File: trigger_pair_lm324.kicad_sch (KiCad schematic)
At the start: 53 parts, among them J6 AudioJack2, J7 AudioJack2, U11 1SS362FV_L3F, U12 1SS362FV_L3F, U13 LM324, U14 1SS362FV_L3F, U15 1SS362FV_L3F, U16 1SS362FV_L3F, U17 1SS362FV_L3F, U18 LM324

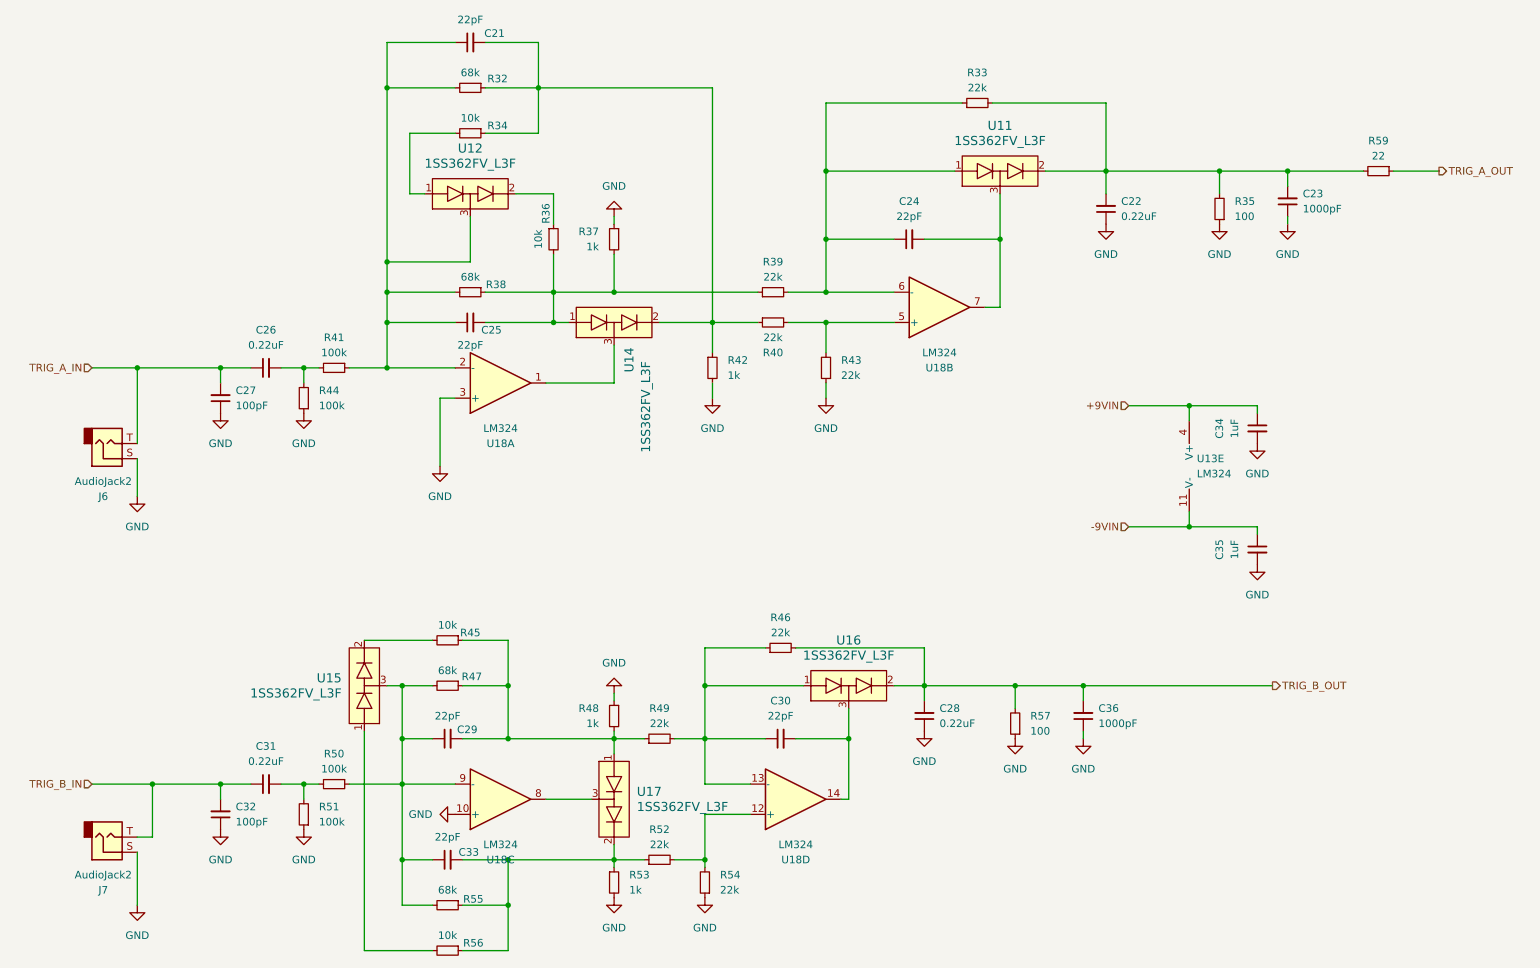
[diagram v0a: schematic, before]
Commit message: Double trigger layout to test
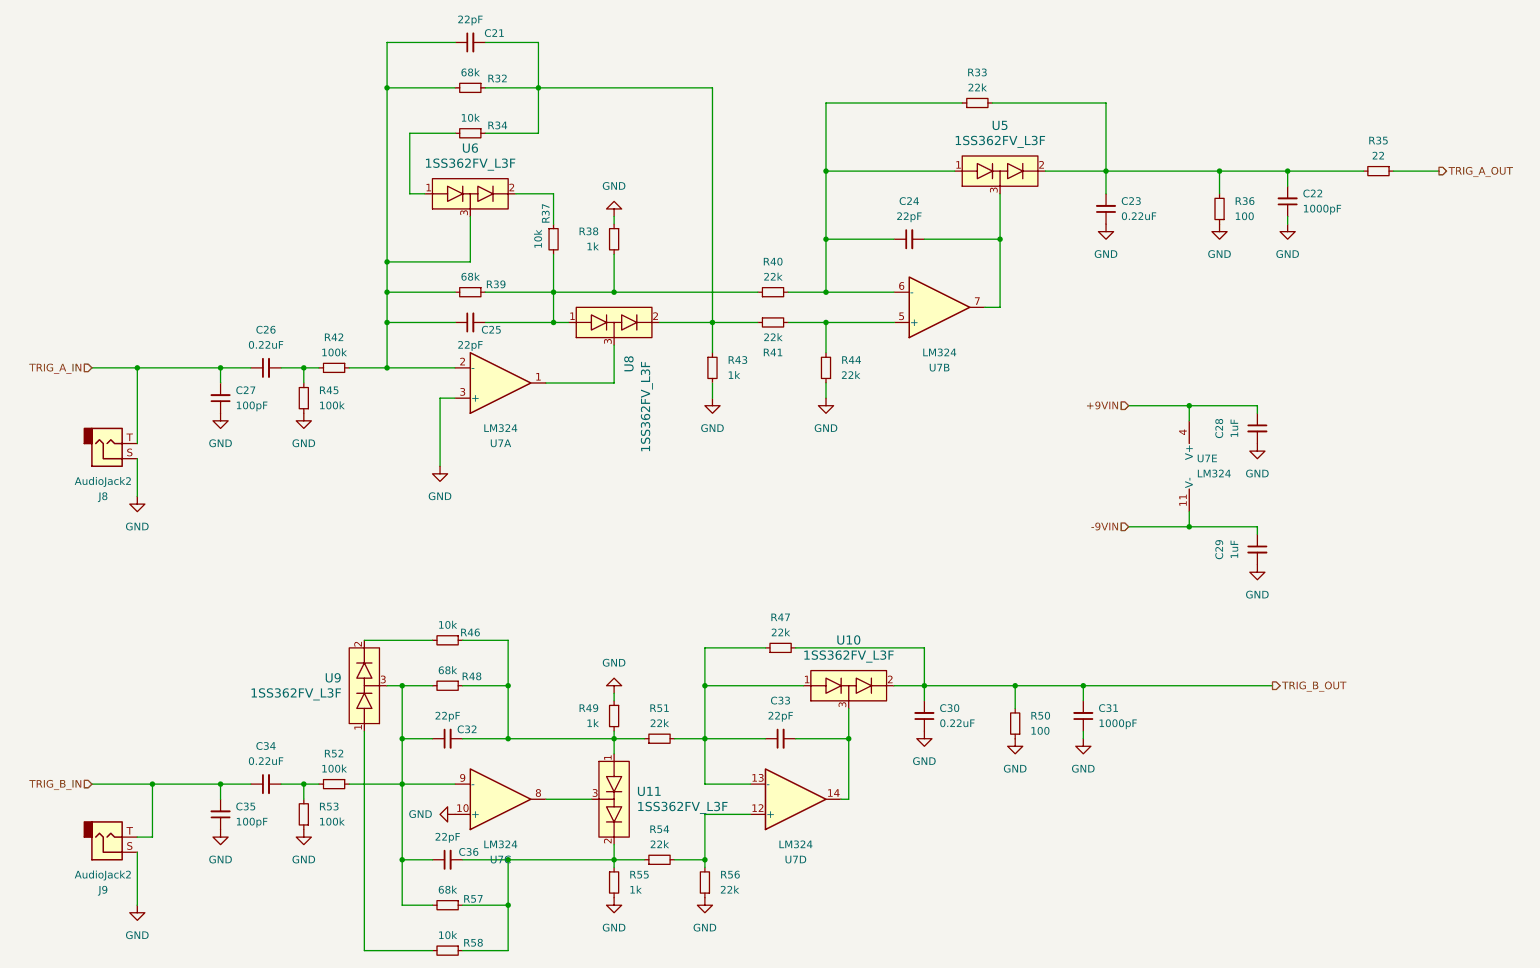
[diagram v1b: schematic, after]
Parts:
- C21, C24, C25: footprint Capacitor_SMD:C_0402_1005Metric -> C_0402_custom:C_0402_1005Metric
- C32: renamed from C29; footprint Capacitor_SMD:C_0402_1005Metric -> C_0402_custom:C_0402_1005Metric
- C33: renamed from C30; footprint Capacitor_SMD:C_0402_1005Metric -> C_0402_custom:C_0402_1005Metric
- C36: renamed from C33; footprint Capacitor_SMD:C_0402_1005Metric -> C_0402_custom:C_0402_1005Metric
- R32, R33, R34: footprint Resistor_SMD:R_0402_1005Metric -> R_0402_custom:R_0402_1005Metric
- R35: renamed from R59; footprint Resistor_SMD:R_0402_1005Metric -> R_0402_custom:R_0402_1005Metric
- R36: renamed from R35; footprint Resistor_SMD:R_0402_1005Metric -> R_0402_custom:R_0402_1005Metric
- R37: renamed from R36; footprint Resistor_SMD:R_0402_1005Metric -> R_0402_custom:R_0402_1005Metric
- R38: renamed from R37; footprint Resistor_SMD:R_0402_1005Metric -> R_0402_custom:R_0402_1005Metric
- R39: renamed from R38; footprint Resistor_SMD:R_0402_1005Metric -> R_0402_custom:R_0402_1005Metric
- R40: renamed from R39; footprint Resistor_SMD:R_0402_1005Metric -> R_0402_custom:R_0402_1005Metric
- R41: renamed from R40; footprint Resistor_SMD:R_0402_1005Metric -> R_0402_custom:R_0402_1005Metric
- R43: renamed from R42; footprint Resistor_SMD:R_0402_1005Metric -> R_0402_custom:R_0402_1005Metric
- R44: renamed from R43; footprint Resistor_SMD:R_0402_1005Metric -> R_0402_custom:R_0402_1005Metric
- R46: renamed from R45; footprint Resistor_SMD:R_0402_1005Metric -> R_0402_custom:R_0402_1005Metric
- R47: renamed from R46; footprint Resistor_SMD:R_0402_1005Metric -> R_0402_custom:R_0402_1005Metric
- R48: renamed from R47; footprint Resistor_SMD:R_0402_1005Metric -> R_0402_custom:R_0402_1005Metric
- R49: renamed from R48; footprint Resistor_SMD:R_0402_1005Metric -> R_0402_custom:R_0402_1005Metric
- R50: renamed from R57; footprint Resistor_SMD:R_0402_1005Metric -> R_0402_custom:R_0402_1005Metric
- R51: renamed from R49; footprint Resistor_SMD:R_0402_1005Metric -> R_0402_custom:R_0402_1005Metric
- R54: renamed from R52; footprint Resistor_SMD:R_0402_1005Metric -> R_0402_custom:R_0402_1005Metric
- R55: renamed from R53; footprint Resistor_SMD:R_0402_1005Metric -> R_0402_custom:R_0402_1005Metric
- R56: renamed from R54; footprint Resistor_SMD:R_0402_1005Metric -> R_0402_custom:R_0402_1005Metric
- R57: renamed from R55; footprint Resistor_SMD:R_0402_1005Metric -> R_0402_custom:R_0402_1005Metric
- R58: renamed from R56; footprint Resistor_SMD:R_0402_1005Metric -> R_0402_custom:R_0402_1005Metric
- renumbered C23 to C22, C22 to C23, C34 to C28, C35 to C29, C28 to C30, C36 to C31, C31 to C34, C32 to C35, J6 to J8, J7 to J9, R41 to R42, R44 to R45, R50 to R52, R51 to R53, U16 to U10, U17 to U11, U11 to U5, U12 to U6, U18 to U7, U13 to U7, U14 to U8, U15 to U9

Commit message: Production ready pcb
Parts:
- C21, C24, C25, C32, C33, C36: LTSC (none) -> C1555
- C22, C31: LTSC (none) -> C1588
- C23, C26, C30, C34: LTSC (none) -> C21120
- C27, C35: LTSC (none) -> C14858
- C28, C29: LTSC (none) -> C15849
- R33, R40, R41, R44, R47, R51, R54, R56: LTSC (none) -> C25768
- R34, R37, R46, R58: LTSC (none) -> C25744
- R35: LTSC (none) -> C25092
- R36, R50: LTSC (none) -> C25076
- R38, R43, R49, R55: LTSC (none) -> C11702
- R42, R45, R52, R53: LTSC (none) -> C25803
- U7: LTSC (none) -> C71035

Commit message: Minor upates to the pcb
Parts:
- C21, C24, C25, C32, C33, C36: LCSC (none) -> C1555; LTSC C1555 -> (none)
- C22, C31: LCSC (none) -> C1588; LTSC C1588 -> (none)
- C23, C26, C30, C34: LCSC (none) -> C21120; LTSC C21120 -> (none)
- C27, C35: LCSC (none) -> C14858; LTSC C14858 -> (none)
- C28, C29: LCSC (none) -> C15849; LTSC C15849 -> (none)
- R33, R40, R41, R44, R47, R51, R54, R56: LCSC (none) -> C25768; LTSC C25768 -> (none)
- R34, R37, R46, R58: LCSC (none) -> C25744; LTSC C25744 -> (none)
- R35: LCSC (none) -> C25092; LTSC C25092 -> (none)
- R36, R50: LCSC (none) -> C25076; LTSC C25076 -> (none)
- R38, R43, R49, R55: LCSC (none) -> C11702; LTSC C11702 -> (none)
- R42, R45, R52, R53: LCSC (none) -> C25803; LTSC C25803 -> (none)
- U7: LCSC (none) -> C71035; LTSC C71035 -> (none)
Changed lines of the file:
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@@
 			)
 		)
-		(property "LTSC" "C11702"
+		(property "LCSC" "C11702"
 			(at 118.11 162.56 0)
 			(effects
@@
 			)
 		)
-		(property "LTSC" "C1555"
+		(property "LCSC" "C1555"
 			(at 93.98 68.58 90)
 			(effects
@@
 			)
 		)
-		(property "LTSC" "C25803"
+		(property "LCSC" "C25803"
 			(at 71.12 76.2 90)
 			(effects
@@
 			)
 		)
-		(property "LTSC" "C25076"
+		(property "LCSC" "C25076"
 			(at 185.42 135.89 0)
 			(effects
@@
 			)
 		)
-		(property "LTSC" ""
-			(at 93.98 29.21 90)
-			(effects
-				(font
-					(size 1.27 1.27)
-				)
-				(hide yes)
-			)
-		)
 		(pin "2"
 		)
@@
 			)
 		)
-		(property "LTSC" "C25744"
+		(property "LCSC" "C25744"
 			(at 90.17 121.92 90)
 			(effects
@@
 			)
 		)
-		(property "LTSC" "C25076"
+		(property "LCSC" "C25076"
 			(at 219.71 49.53 0)
 			(effects
@@
 			)
 		)
-		(property "LTSC" "C25092"
+		(property "LCSC" "C25092"
 			(at 246.38 43.18 90)
 			(effects
@@
 			)
 		)
-		(property "LTSC" "C25768"
+		(property "LCSC" "C25768"
 			(at 133.35 162.56 0)
 			(effects
@@
 			)
 		)
-		(property "LTSC" "C11702"
+		(property "LCSC" "C11702"
 			(at 118.11 134.62 0)
 			(effects
@@
 			)
 		)
-		(property "LTSC" "C25768"
+		(property "LCSC" "C25768"
 			(at 125.73 158.75 90)
 			(effects
@@
 			)
 		)
-		(property "LTSC" "C1555"
+		(property "LCSC" "C1555"
 			(at 90.17 158.75 90)
 			(effects
@@
 			)
 		)
-		(property "LTSC" "C71035"
+		(property "LCSC" "C71035"
 			(at 148.59 148.59 0)
 			(effects
@@
 			)
 		)
-		(property "LTSC" ""
-			(at 33.02 88.9 0)
-			(effects
-				(font
-					(size 1.27 1.27)
-				)
-				(hide yes)
-			)
-		)
 		(pin "T"
 		)
@@
 			)
 		)
-		(property "LTSC" "C1555"
+		(property "LCSC" "C1555"
 			(at 146.05 138.43 90)
 			(effects
@@
 			)
 		)
-		(property "LTSC" "C71035"
+		(property "LCSC" "C71035"
 			(at 172.72 66.04 0)
 			(effects
@@
 			)
 		)
-		(property "LTSC" "C25768"
+		(property "LCSC" "C25768"
 			(at 125.73 138.43 90)
 			(effects
@@
 			)
 		)
-		(property "LTSC" "C25803"
+		(property "LCSC" "C25803"
 			(at 71.12 146.05 90)
 			(effects
@@
 			)
 		)
-		(property "LTSC" "C71035"
+		(property "LCSC" "C71035"
 			(at 99.06 78.74 0)
 			(effects
@@
 			)
 		)
-		(property "LTSC" "C25768"
+		(property "LCSC" "C25768"
 			(at 144.78 63.5 90)
 			(effects
@@
 			)
 		)
-		(property "LTSC" "C21120"
+		(property "LCSC" "C21120"
 			(at 59.69 146.05 90)
 			(effects
@@
 			)
 		)
-		(property "LTSC" ""
-			(at 93.98 63.5 90)
-			(effects
-				(font
-					(size 1.27 1.27)
-				)
-				(hide yes)
-			)
-		)
 		(pin "2"
 		)
@@
 			)
 		)
-		(property "LTSC" "C25768"
+		(property "LCSC" "C25768"
 			(at 153.67 76.2 0)
 			(effects
@@
 			)
 		)
-		(property "LTSC" "C15849"
+		(property "LCSC" "C15849"
 			(at 226.06 106.68 90)
 			(effects
@@
 			)
 		)
-		(property "LTSC" ""
-			(at 76.2 129.54 90)
-			(effects
-				(font
-					(size 1.27 1.27)
-				)
-				(hide yes)
-			)
-		)
 		(pin "3"
 		)
@@
 			)
 		)
-		(property "LTSC" ""
-			(at 33.02 154.94 0)
-			(effects
-				(font
-					(size 1.27 1.27)
-				)
-				(hide yes)
-			)
-		)
 		(pin "T"
 		)
@@
 			)
 		)
-		(property "LTSC" ""
-			(at 157.48 129.54 0)
-			(effects
-				(font
-					(size 1.27 1.27)
-				)
-				(hide yes)
-			)
-		)
 		(pin "3"
 		)
@@
 			)
 		)
-		(property "LTSC" "C71035"
+		(property "LCSC" "C71035"
 			(at 217.17 92.71 0)
 			(effects
@@
 			)
 		)
-		(property "LTSC" "C15849"
+		(property "LCSC" "C15849"
 			(at 226.06 86.36 90)
 			(effects
@@
 			)
 		)
-		(property "LTSC" ""
-			(at 93.98 46.99 0)
-			(effects
-				(font
-					(size 1.27 1.27)
-				)
-				(hide yes)
-			)
-		)
 		(pin "3"
 		)
@@
 			)
 		)
-		(property "LTSC" "C14858"
+		(property "LCSC" "C14858"
 			(at 52.07 151.13 0)
 			(effects
@@
 			)
 		)
-		(property "LTSC" ""
-			(at 90.17 129.54 90)
-			(effects
-				(font
-					(size 1.27 1.27)
-				)
-				(hide yes)
-			)
-		)
 		(pin "2"
 		)
@@
 			)
 		)
-		(property "LTSC" "C25744"
+		(property "LCSC" "C25744"
 			(at 93.98 36.83 90)
 			(effects
@@
 			)
 		)
-		(property "LTSC" ""
-			(at 90.17 166.37 90)
-			(effects
-				(font
-					(size 1.27 1.27)
-				)
-				(hide yes)
-			)
-		)
 		(pin "2"
 		)
@@
 			)
 		)
-		(property "LTSC" "C1588"
+		(property "LCSC" "C1588"
 			(at 231.14 48.26 0)
 			(effects
@@
 			)
 		)
-		(property "LTSC" "C1588"
+		(property "LCSC" "C1588"
 			(at 196.85 134.62 0)
 			(effects
@@
 			)
 		)
-		(property "LTSC" "C21120"
+		(property "LCSC" "C21120"
 			(at 200.66 49.53 0)
 			(effects
@@
 			)
 		)
-		(property "LTSC" "C25744"
+		(property "LCSC" "C25744"
 			(at 107.95 54.61 90)
 			(effects
@@
 			)
 		)
-		(property "LTSC" "C21120"
+		(property "LCSC" "C21120"
 			(at 170.18 134.62 0)
 			(effects
@@
 			)
 		)
-		(property "LTSC" "C1555"
+		(property "LCSC" "C1555"
 			(at 167.64 54.61 90)
 			(effects
@@
 			)
 		)
-		(property "LTSC" "C25768"
+		(property "LCSC" "C25768"
 			(at 179.07 31.75 90)
 			(effects
@@
 			)
 		)
-		(property "LTSC" ""
-			(at 118.11 148.59 90)
-			(effects
-				(font
-					(size 1.27 1.27)
-				)
-				(hide yes)
-			)
-		)
 		(pin "3"
 		)
@@
 			)
 		)
-		(property "LTSC" "C21120"
+		(property "LCSC" "C21120"
 			(at 59.69 76.2 90)
 			(effects
@@
 			)
 		)
-		(property "LTSC" "C71035"
+		(property "LCSC" "C71035"
 			(at 99.06 148.59 0)
 			(effects
@@
 			)
 		)
-		(property "LTSC" "C25744"
+		(property "LCSC" "C25744"
 			(at 90.17 173.99 90)
 			(effects
@@
 			)
 		)
-		(property "LTSC" "C25768"
+		(property "LCSC" "C25768"
 			(at 146.05 123.19 90)
 			(effects
@@
 			)
 		)
-		(property "LTSC" "C11702"
+		(property "LCSC" "C11702"
 			(at 118.11 54.61 0)
 			(effects
@@
 			)
 		)
-		(property "LTSC" "C1555"
+		(property "LCSC" "C1555"
 			(at 90.17 138.43 90)
 			(effects
@@
 			)
 		)
-		(property "LTSC" "C11702"
+		(property "LCSC" "C11702"
 			(at 134.62 76.2 0)
 			(effects
@@
 			)
 		)
-		(property "LTSC" "C14858"
+		(property "LCSC" "C14858"
 			(at 52.07 81.28 0)
 			(effects
@@
 			)
 		)
-		(property "LTSC" "C25803"
+		(property "LCSC" "C25803"
 			(at 66.04 151.13 0)
 			(effects
@@
 			)
 		)
-		(property "LTSC" "C25803"
+		(property "LCSC" "C25803"
 			(at 66.04 81.28 0)
 			(effects
@@
 			)
 		)
-		(property "LTSC" ""
-			(at 182.88 43.18 0)
-			(effects
-				(font
-					(size 1.27 1.27)
-				)
-				(hide yes)
-			)
-		)
 		(pin "3"
 		)
@@
 			)
 		)
-		(property "LTSC" "C25768"
+		(property "LCSC" "C25768"
 			(at 144.78 68.58 90)
 			(effects
@@
 			)
 		)
-		(property "LTSC" ""
-			(at 118.11 68.58 90)
-			(effects
-				(font
-					(size 1.27 1.27)
-				)
-				(hide yes)
-			)
-		)
 		(pin "3"
 		)
@@
 			)
 		)
-		(property "LTSC" "C1555"
+		(property "LCSC" "C1555"
 			(at 93.98 21.59 90)
 			(effects

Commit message: Simulation fixes + board fixes
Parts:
- removed C21, C24, C25, C32, C33, C36: 22pF, C_0402_custom:C_0402_1005Metric, symbol Device:C_Small
- removed C22, C31: 1000pF, Capacitor_SMD:C_0603_1608Metric, symbol Device:C_Small
- removed C23, C26, C30, C34: 0.22uF, Capacitor_SMD:C_0603_1608Metric, symbol Device:C_Small
- removed C27, C35: 100pF, Capacitor_SMD:C_0603_1608Metric, symbol Device:C_Small
- removed C28, C29: 1uF, Capacitor_SMD:C_0603_1608Metric, symbol Device:C_Small
- removed J8, J9: AudioJack2, Connector_Audio:Jack_6.35mm_Neutrik_NMJ4HCD2_Horizontal, symbol Connector_Audio:AudioJack2
- removed R32, R39, R48, R57: 68k, R_0402_custom:R_0402_1005Metric, symbol Device:R_Small
- removed R33, R40, R41, R44, R47, R51, R54, R56: 22k, R_0402_custom:R_0402_1005Metric, symbol Device:R_Small
- removed R34, R37, R46, R58: 10k, R_0402_custom:R_0402_1005Metric, symbol Device:R_Small
- removed R35: 22, R_0402_custom:R_0402_1005Metric, symbol Device:R_Small
- removed R36, R50: 100, R_0402_custom:R_0402_1005Metric, symbol Device:R_Small
- removed R38, R43, R49, R55: 1k, R_0402_custom:R_0402_1005Metric, symbol Device:R_Small
- removed R42, R45, R52, R53: 100k, Resistor_SMD:R_0603_1608Metric, symbol Device:R_Small
- removed U10, U11, U5, U6, U8, U9: 1SS362FV_L3F, mod:DIODE_1SS362FV, symbol DIODE_SET_1SS362FV:1SS362FV_L3F
- removed U7: LM324, Package_SO:SOIC-14_3.9x8.7mm_P1.27mm, symbol Amplifier_Operational:LM324
